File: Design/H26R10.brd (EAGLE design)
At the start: 34.6 x 30 mm, 39 parts, among them P1 HEXABIT_17.32_NO_P3_P6_P7_P12, P2 CON-PHOENIX-350_1751277, P3 1751251, U1 STM32F091CBU6, U2 AD8295BCPZ-WP, U3 AD8275BRMZ, U4 AD7687BRMZ, U5 ADR431ARMZ, X1 XTALL_CSTCE8M00G52

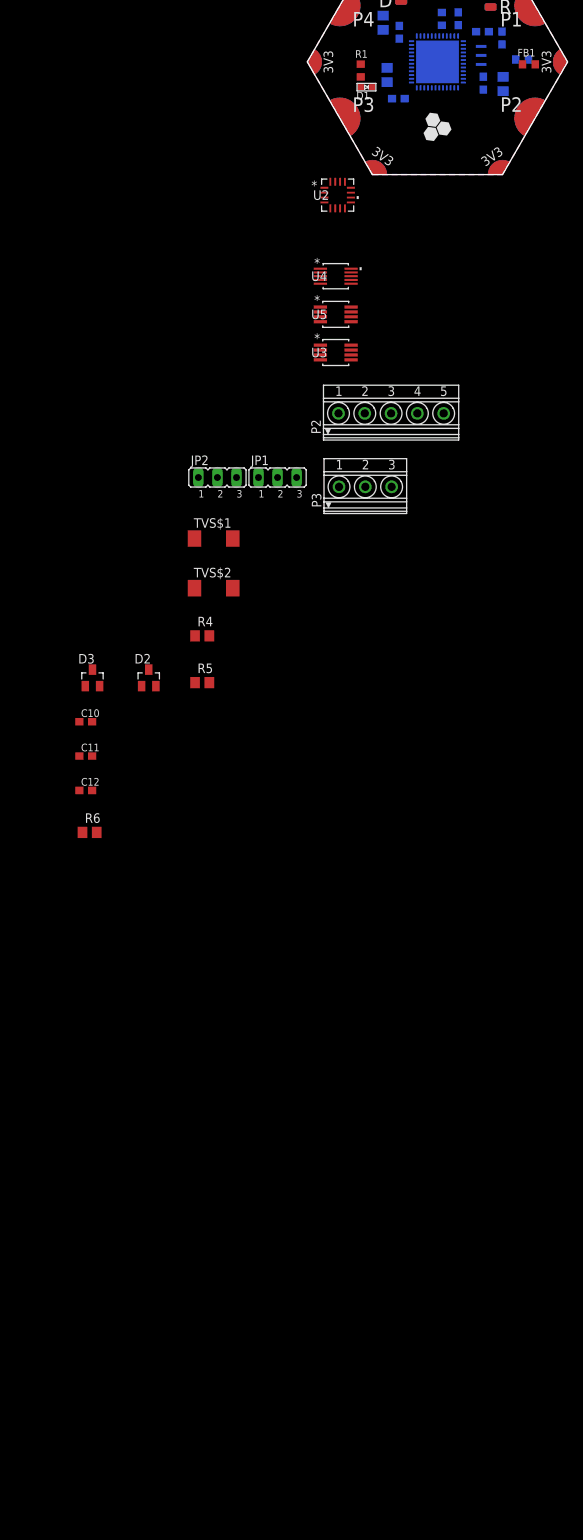
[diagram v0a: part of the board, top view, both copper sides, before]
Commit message: Finished analog power chain and some AD8295 connections
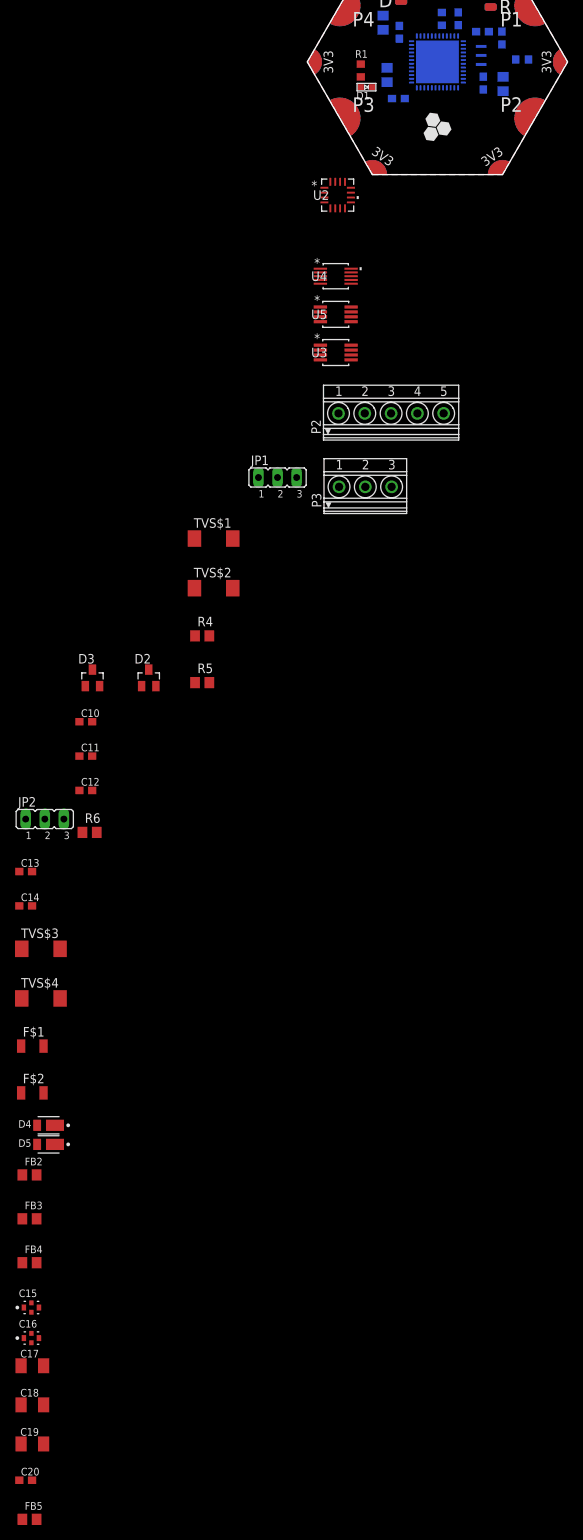
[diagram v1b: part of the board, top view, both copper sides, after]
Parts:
- removed FB1: FB-TDK_MMZ1608Y300B, Hexabitz:FB-TDK_MMZ1608Y300B
- added C13, C14, C20: 100nF, Hexabitz:C-0603
- added C15, C16: MURATA_NFM21PC105B1A3DMURATA_NFM21PC105B1A3D_0_0, Hexabitz:MURATA_NFM21PC105B1A3D_0
- added C17, C18, C19: 10uF, Hexabitz:C1206K
- added D4, D5: DIODES_SBR2U30P1-7DIODES_SBR2U30P1-7_0_0, Hexabitz:DIODES_SBR2U30P1-7_0
- added F$1, F$2: NANOSMDC035F-2120, Hexabitz:R1206
- added FB2, FB3, FB4, FB5: 330@100MHz, Hexabitz:FB-0805
- added TVS$3, TVS$4: SMBJ30CA, Hexabitz:DO214AA
- moved JP2 50.9 mm to (-17.7, -66.2)
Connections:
- removed net VDDA: C1.1, C2.1, FB1.1, U1.P$9
- new net +5V: U5.6
- new net AD8295_A1O: U2.7
- new net AD8295_A2O: U2.12
- new net AD8295_OUT: U2.15
- new net N$15: F$1.1, P3.3
- new net N$16: F$2.1, P3.1
- new net N$17: D4.2, F$1.2, TVS$3.C
- new net N$18: D5.1, F$2.2, TVS$4.A
- new net N$19: FB3.1, P3.2, TVS$3.A, TVS$4.C
- new net N$20: D4.1, FB2.1
- new net N$21: D5.2, FB4.1
- new net N$22: C15.1, FB2.2
- new net N$23: C16.3, FB4.2
- new net N$24: C17.2, C18.1, FB3.2
- net +15V: now also C13.1, C15.3, C17.1, C19.1, C20.1, U5.2
- net -15V: now also C14.1, C16.1, C18.2
- net AGND: now also C13.2, C14.2, C19.2, C20.2, FB5.2, U2.6, U5.4
- net GND: now also C1.2, C2.2, FB5.1, U1.P$8
- net VDD: now also C1.1, C2.1, U1.P$9; no longer FB1.2
- net VSSA: no longer C1.2, C2.2, U1.P$8

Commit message: Finished schematics. No ERC yet
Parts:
- removed R2: 0.0R, Hexabitz:R-0603
- added C21, C22, C23, C27: 100nF, Hexabitz:C-0603
- added C24: 1.5nF, Hexabitz:C-0603
- added C25: 22uF, Hexabitz:C1206K
- added R10, R9: 33.0, Hexabitz:R-0805
- added R11: 0.0R, Hexabitz:R-0603
- added R7, R8: 1.00K, Hexabitz:R-0805
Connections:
- net UART2_RX renamed UART2_RX*
- net UART2_TX renamed UART2_TX*
- removed net VIO: U4.10
- removed net VS+: U3.7
- removed net VS-: U3.4
- removed net VSSA: R2.2
- new net AD8295_A1R1: R9.1, U2.10, U3.5, U3.6
- new net N$25: C21.2, R7.2, R8.1, U2.11
- new net N$26: R11.2, U4.9
- new net N$27: C24.1, R9.2, U4.3
- new net N$28: C24.2, R10.2, U4.4
- new net N$29: P1.PAD_PU1
- new net N$30: P1.PAD_PU2
- new net N$31: P1.PAD_PD1
- new net N$32: P1.PAD_PD2
- new net N$33: P1.PAD_PU4
- new net N$34: P1.PAD_PU5
- new net N$35: P1.PAD_PD4
- new net N$36: P1.PAD_PD5
- new net SPI2_CS: U1.P$25, U4.6
- new net SPI2_MISO: U1.P$27, U4.7
- new net SPI2_SCK: U1.P$26, U4.8
- net +15V: now also C22.1, U3.7
- net +5V: now also C23.1, C25.1, R7.1, U2.14, U4.1
- net AD8295_A1O: now also R10.1, U2.8, U3.1, U3.8
- net AD8295_A2O: now also U4.2
- net AD8295_OUT: now also U3.3
- net AGND: now also C21.1, C22.2, C23.2, C25.2, R8.2, U2.13, U3.2, U3.4, U4.5
- net GND: now also C27.2; no longer R2.1
- net VDD: now also C27.1, R11.1, U4.10; no longer U4.2

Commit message: Renumber schematics Arrange analong path in PCB to estimate footprint Replace module connector with double hexagon Need to replace MCU with bigger package to use 8 UARTs
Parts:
- removed C22: 100nF, Hexabitz:C-0603
- removed F$1, F$2: NANOSMDC035F-2120, Hexabitz:R1206
- removed FB5: 330@100MHz, Hexabitz:FB-0805
- removed P2: CON-PHOENIX-350_1751277, Hexabitz:CON-PHOENIX-350_1751277
- removed P3: 1751251, con-phoenix-350:1751251
- removed R11: 0.0R, Hexabitz:R-0603
- removed TVS$1, TVS$2, TVS$3, TVS$4: SMBJ30CA, Hexabitz:DO214AA
- added C26: 100nF, Hexabitz:C-0603
- added F1, F2: NANOSMDC035F-2120, Hexabitz:R1206
- added FB1: 330@100MHz, Hexabitz:FB-0805
- added R2: 10.0K, Hexabitz:R-0603
- added TVS1, TVS2, TVS3, TVS4: SMBJ30CA, Hexabitz:DO214AA
- added X2: 1751251, con-phoenix-350:1751251
- added X3: CON-PHOENIX-350_1751277, Hexabitz:CON-PHOENIX-350_1751277
- C10: value 1nF -> 100nF
- C11, C12: value 100pF -> MURATA_NFM21PC105B1A3DMURATA_NFM21PC105B1A3D_0_0; device Hexabitz:C-0603 -> Hexabitz:MURATA_NFM21PC105B1A3D_0
- C13, C14: value 100nF -> 10uF; device Hexabitz:C-0603 -> Hexabitz:C1206K
- C15: value MURATA_NFM21PC105B1A3DMURATA_NFM21PC105B1A3D_0_0 -> 100pF; device Hexabitz:MURATA_NFM21PC105B1A3D_0 -> Hexabitz:C-0603
- C16: value MURATA_NFM21PC105B1A3DMURATA_NFM21PC105B1A3D_0_0 -> 1nF; device Hexabitz:MURATA_NFM21PC105B1A3D_0 -> Hexabitz:C-0603
- C17: value 10uF -> 100pF; device Hexabitz:C1206K -> Hexabitz:C-0603
- C19: value 10uF -> 100nF; device Hexabitz:C1206K -> Hexabitz:C-0603
- C21: value 100nF -> 1.5nF
- C24: value 1.5nF -> 100nF
- D2, D3: value BAT54S -> DIODES_SBR2U30P1-7DIODES_SBR2U30P1-7_0_0; device Hexabitz:SOT23 -> Hexabitz:DIODES_SBR2U30P1-7_0
- D4, D5: value DIODES_SBR2U30P1-7DIODES_SBR2U30P1-7_0_0 -> BAT54S; device Hexabitz:DIODES_SBR2U30P1-7_0 -> Hexabitz:SOT23
- P1: value HEXABIT_17.32_NO_P3_P6_P7_P12 -> HEXABIT_17.32_X2_NO_P5_P10_P11_P20; device hexabitz_connectors:HEXABIT_17.32_NO_P3_P6_P7_P12 -> hexabitz_connectors:HEXABIT_17.32_X2_NO_P5_P10_P11_P20
- R10: value 33.0 -> 0.0R; device Hexabitz:R-0805 -> Hexabitz:R-0603
- R3: value 10.0K -> 1.50K; device Hexabitz:R-0603 -> Hexabitz:R-0805
- R5: value 1.50K -> 1.00K
- R6: value DNP -> 1.00K
- R7, R8: value 1.00K -> 33.0
- R9: value 33.0 -> DNP
- U2: value AD8295BCPZ-WP -> AD8275BRMZ; device Hexabitz:CP_16_19 -> Hexabitz:RM_8
- U3: value AD8275BRMZ -> ADR431ARMZ
- U4: value AD7687BRMZ -> AD8295BCPZ-WP; device Hexabitz:RM_10 -> Hexabitz:CP_16_19
- U5: value ADR431ARMZ -> AD7687BRMZ; device Hexabitz:RM_8 -> Hexabitz:RM_10
- moved C24 261.6 mm to (79.5, 38.6), turned to 90 degrees
- moved C27 256.5 mm to (79.4, 18.7)
- moved R9 251.0 mm to (75.1, 40.6)
- moved C25 242.9 mm to (80.6, 13.1), turned to 180 degrees
- moved R10 230.2 mm to (71.9, 13.2), turned to 90 degrees
- moved C23 222.9 mm to (71.9, 16.8), turned to 90 degrees
- moved C21 219.4 mm to (75.3, 20.4)
- moved R8 218.4 mm to (77.1, 24.0), turned to 270 degrees
- moved C20 216.1 mm to (90.8, 31.2), turned to 270 degrees
- moved FB4 211.3 mm to (102.9, 46.9)
- moved R7 211.2 mm to (73.3, 24.0), turned to 270 degrees
- moved C19 205.7 mm to (79.6, 31.0), turned to 90 degrees
- moved C17 204.1 mm to (70.7, 44.2), turned to 180 degrees
- moved C16 202.7 mm to (74.9, 44.2), turned to 180 degrees
- moved C18 202.6 mm to (82.4, 31.1), turned to 90 degrees
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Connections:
- removed net N$31: P1.PAD_PD1
- removed net N$32: P1.PAD_PD2
- removed net N$33: P1.PAD_PU4
- removed net N$35: P1.PAD_PD4
- removed net N$36: P1.PAD_PD5
- net +15V: now also C10.1, C11.3, C18.1, C24.1, D4.2, D5.2, U2.7, U3.2, U4.16, X3.5; no longer C15.3, C17.1, C20.1, C22.1, D2.2, D3.2, P2.5, U2.16, U3.7, U5.2
- net +5V: now also R5.1, U3.6, U4.14, U5.1; no longer C23.1, R7.1, U2.14, U4.1, U5.6
- net -15V: now also C12.1, C14.2, C26.1, D4.1, D5.1, U4.5, X3.4; no longer C14.1, C16.1, C18.2, D2.1, D3.1, P2.4, U2.5
- net AD8295_A1O: now also R8.1, U2.1, U4.7, U4.8; no longer R10.1, U2.7, U3.1, U3.8
- net AD8295_A1R1: now also R7.1, U2.5, U2.6, U4.10; no longer R9.1, U2.10, U3.5, U3.6
- net AD8295_A2O: now also C27.1, U4.12, U5.2; no longer U2.12, U4.2
- net AD8295_OUT: now also U2.3, U4.15; no longer U2.15, U3.3
- net AGND: now also C10.2, C15.1, C17.2, C18.2, C20.1, C24.2, C26.2, C27.2, FB4.2, R6.2, TVS3.A, TVS4.A, U2.2, U2.4, U4.13, U4.6, U5.5, X3.1; no longer C11.2, C12.1, C13.2, C14.2, C20.2, C21.1, C22.2, C23.2, FB5.2, P2.1, R8.2, TVS$1.A, TVS$2.A, U2.13, U2.6, U3.2, U4.5, U5.4
- net B1: now also R2.2; no longer R3.2
- net GND: now also C23.2, FB4.1, P1.PAD_PD12, P1.PAD_PD13, P1.PAD_PD14, P1.PAD_PD15, P1.PAD_PD16, P1.PAD_PD17, P1.PAD_PD18, P1.PAD_PD19, R2.1; no longer C27.2, FB5.1, P1.PAD_PD10, P1.PAD_PD11, P1.PAD_PD8, P1.PAD_PD9, R3.1
- net N$1: now also JP2.1, X3.3; no longer JP1.1, P2.3
- net N$10: now also JP1.2, R4.1, TVS3.C; no longer JP2.2, R5.1, TVS$2.C
- net N$11: now also C15.2, C16.1, D4.3, R3.2, U4.1; no longer C10.1, C12.2, D2.3, R4.2, U2.1
- net N$12: now also C16.2, C17.1, D5.3, R4.2, U4.4; no longer C10.2, C11.1, D3.3, R5.2, U2.4
- net N$13: now also R9.2, U4.2; no longer R6.2, U2.2
- net N$14: now also R9.1, U4.3; no longer R6.1, U2.3
- net N$15: now also F1.1, X2.3; no longer F$1.1, P3.3
- net N$16: now also F2.1, X2.1; no longer F$2.1, P3.1
- net N$17: now also D2.2, F1.2, TVS1.C; no longer D4.2, F$1.2, TVS$3.C
- net N$18: now also D3.1, F2.2, TVS2.A; no longer D5.1, F$2.2, TVS$4.A
- net N$19: now also FB2.1, TVS1.A, TVS2.C, X2.2; no longer FB3.1, P3.2, TVS$3.A, TVS$4.C
- net N$2: now also JP1.1, X3.2; no longer JP2.1, P2.2
- net N$20: now also D2.1, FB1.1; no longer D4.1, FB2.1
- net N$21: now also D3.2, FB3.1; no longer D5.2, FB4.1
- net N$22: now also C11.1, FB1.2; no longer C15.1, FB2.2
- net N$23: now also C12.3, FB3.2; no longer C16.3, FB4.2
- net N$24: now also C13.2, C14.1, FB2.2; no longer C17.2, C18.1, FB3.2
- net N$25: now also C20.2, R5.2, R6.1, U4.11; no longer C21.2, R7.2, R8.1, U2.11
- net N$26: now also R10.2, U5.9; no longer R11.2, U4.9
- net N$27: now also C21.1, R7.2, U5.3; no longer C24.1, R9.2, U4.3
- net N$28: now also C21.2, R8.2, U5.4; no longer C24.2, R10.2, U4.4
- net N$34: now also P1.PAD_PD1, P1.PAD_PD2, P1.PAD_PD3, P1.PAD_PD4, P1.PAD_PD6, P1.PAD_PD7, P1.PAD_PD8, P1.PAD_PD9, P1.PAD_PU3, P1.PAD_PU4, P1.PAD_PU6, P1.PAD_PU7, P1.PAD_PU8, P1.PAD_PU9; no longer P1.PAD_PU5
- net N$8: now also JP2.2, R3.1, TVS4.C; no longer JP1.2, R4.1, TVS$1.C
- net SPI2_CS: now also U5.6; no longer U4.6
- net SPI2_MISO: now also U5.7; no longer U4.7
- net SPI2_SCK: now also U5.8; no longer U4.8
- net VDD: now also C23.1, P1.PAD_PU12, P1.PAD_PU13, P1.PAD_PU14, P1.PAD_PU15, P1.PAD_PU16, P1.PAD_PU17, P1.PAD_PU18, P1.PAD_PU19, R10.1, U5.10; no longer C27.1, P1.PAD_PU10, P1.PAD_PU11, P1.PAD_PU8, P1.PAD_PU9, R11.1, U4.10
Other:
- board size 34.6 x 30 mm -> 34.6 x 60 mm
- board text added: "P2*"
- board text removed: "P2"

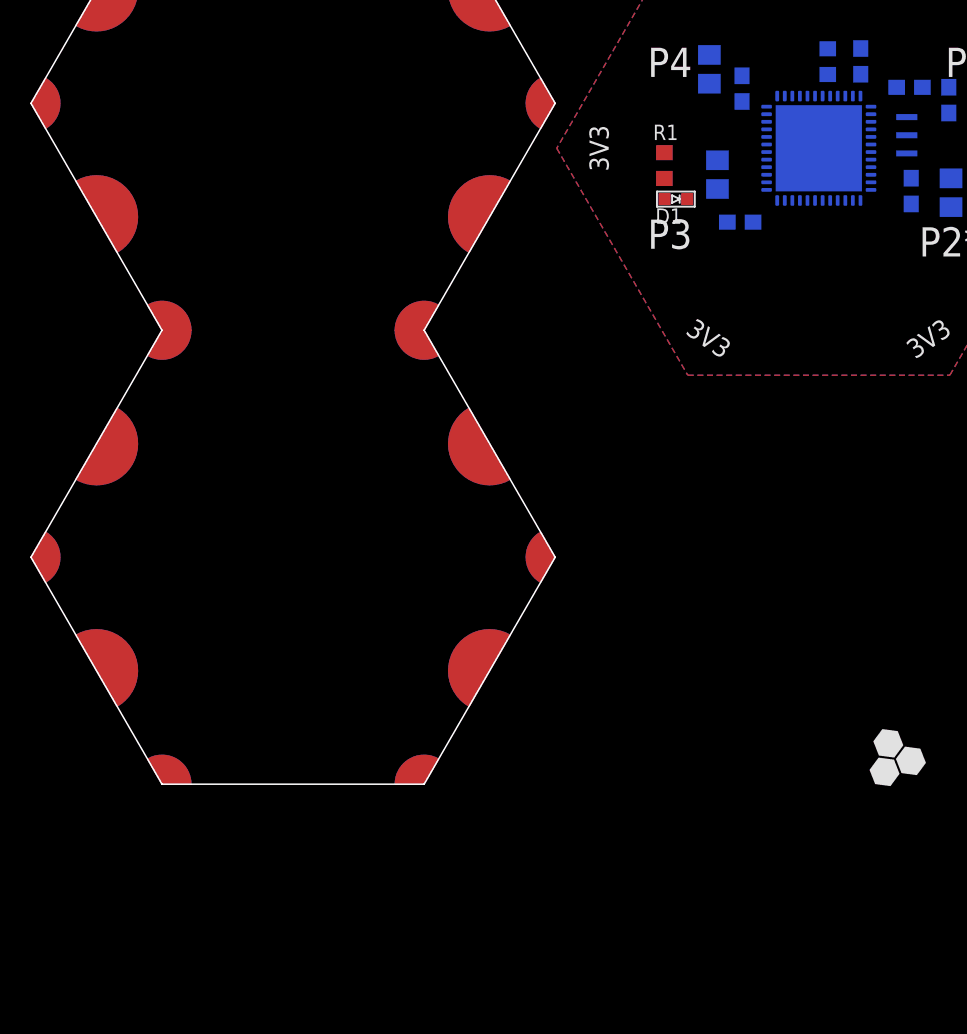
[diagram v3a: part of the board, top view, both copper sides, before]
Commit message: Replace MCU with Add STM32F091RB (LQFP64) and connect UARTs
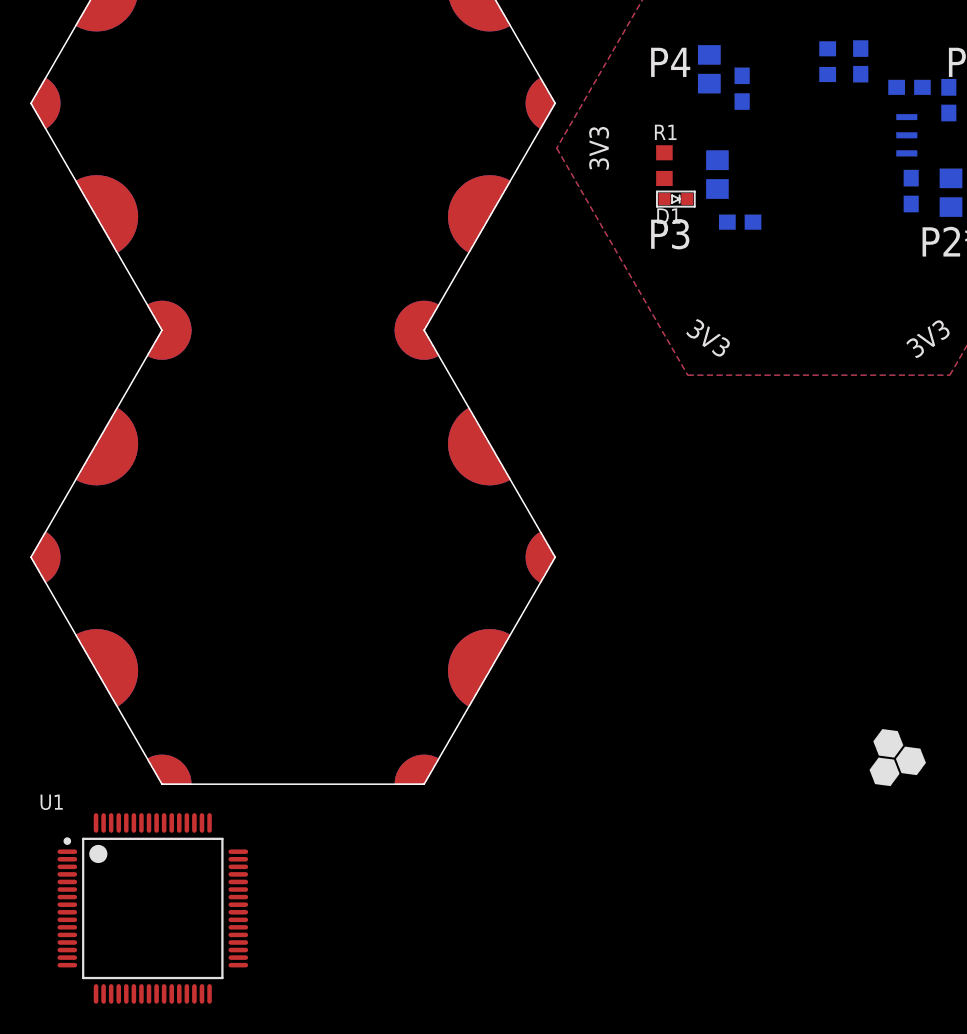
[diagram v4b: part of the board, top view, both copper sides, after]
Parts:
- U1: value STM32F091CBU6 -> STM32F091RBT6STMICROELECTRONICS_STM32F091RBT6_0_1; device Hexabitz:STM32F091CBU6 -> Hexabitz:STMICROELECTRONICS_STM32F091RBT6_1
- moved U1 66.8 mm to (-9.40, -15.6), flipped to the top, turned to 0 degrees
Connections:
- new net UART7_RX: U1.9
- new net UART7_TX: U1.8
- new net UART8_RX: U1.11
- new net UART8_TX: U1.10
- net B1: now also U1.60; no longer U1.P$44
- net GND: now also U1.12, U1.18, U1.31, U1.47, U1.63; no longer U1.EP, U1.P$23, U1.P$35, U1.P$47, U1.P$8
- net N$3: now also U1.44; no longer U1.P$32
- net N$5: now also U1.5; no longer U1.P$5
- net N$6: now also U1.6; no longer U1.P$6
- net N$7: now also U1.46; no longer U1.P$34
- net N$9: now also U1.49; no longer U1.P$37
- net R1: now also U1.7; no longer U1.P$7
- net SPI2_CS: now also U1.33; no longer U1.P$25
- net SPI2_MISO: now also U1.35; no longer U1.P$27
- net SPI2_SCK: now also U1.34; no longer U1.P$26
- net UART1_RX: now also U1.43; no longer U1.P$31
- net UART1_TX: now also U1.42; no longer U1.P$30
- net UART2_RX*: now also U1.17; no longer U1.P$13
- net UART2_TX*: now also U1.16; no longer U1.P$12
- net UART3_RX: now also U1.30; no longer U1.P$22
- net UART3_TX: now also U1.29; no longer U1.P$21
- net UART4_RX: now also U1.15; no longer U1.P$11
- net UART4_TX: now also U1.14; no longer U1.P$10
- net UART5_RX: now also U1.56; no longer U1.P$40
- net UART5_TX: now also U1.55; no longer U1.P$39
- net UART6_RX: now also U1.21; no longer U1.P$15
- net UART6_TX: now also U1.20; no longer U1.P$14
- net VDD: now also U1.1, U1.13, U1.19, U1.32, U1.48, U1.64; no longer U1.P$1, U1.P$24, U1.P$36, U1.P$48, U1.P$9
